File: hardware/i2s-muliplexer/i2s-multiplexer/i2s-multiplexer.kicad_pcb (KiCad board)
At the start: 2 copper layers, 81 x 53.6 mm, 24 parts, among them J1 Conn_01x05, J2 Conn_01x05, J3 Conn_01x05, J4 Conn_01x05, J5 Conn_01x05, J6 Conn_01x07, J7 Conn_01x05, U1 74HC126, U2 74HC126, U3 74HC126, U4 74HC126, U5 74HC126, U6 74HC126, U7 74LS138

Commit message: Added test point
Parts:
- removed the REF** at (96.5, 35.6)
- removed the REF** at (24.6, 35.6)
- removed the REF** at (24.1, 79.8)
- removed the REF** at (96.3, 80.0)
- added REF**: MountingHole_3.2mm_M3_ISO7380, MountingHole:MountingHole_3.2mm_M3_ISO7380, F.Cu at (24.4, 80.0)
- added REF**: MountingHole_3.2mm_M3_ISO7380, MountingHole:MountingHole_3.2mm_M3_ISO7380, F.Cu at (24.4, 34.0)
- added REF**: MountingHole_3.2mm_M3_ISO7380, MountingHole:MountingHole_3.2mm_M3_ISO7380, F.Cu at (98.0, 35.6)
- added REF**: MountingHole_3.2mm_M3_ISO7380, MountingHole:MountingHole_3.2mm_M3_ISO7380, F.Cu at (98.0, 80.0)
- added TP1: TP_GND, Connector_PinHeader_2.54mm:PinHeader_1x01_P2.54mm_Vertical, F.Cu at (86.6, 37.1)
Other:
- board size 81 x 53.6 mm -> 80.5 x 53.6 mm
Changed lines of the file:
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@@
     (tracks 546)
     (zones 0)
-    (modules 24)
+    (modules 25)
     (nets 46)
   )
@@
   )
   (module MountingHole:MountingHole_3.2mm_M3_ISO7380 (layer F.Cu)
-    (at 96.52 35.56)
+    (at 24.384 80.01)
     (descr "Mounting Hole 3.2mm, no annular, M3, ISO7380")
     (tags "mounting hole 3.2mm no annular m3 iso7380")
@@
   )
   (module MountingHole:MountingHole_3.2mm_M3_ISO7380 (layer F.Cu)
-    (at 24.638 35.56)
+    (at 24.384 34.036)
     (descr "Mounting Hole 3.2mm, no annular, M3, ISO7380")
     (tags "mounting hole 3.2mm no annular m3 iso7380")
@@
   )
   (module MountingHole:MountingHole_3.2mm_M3_ISO7380 (layer F.Cu)
-    (at 24.13 79.756)
+    (at 98.044 35.56)
     (descr "Mounting Hole 3.2mm, no annular, M3, ISO7380")
     (tags "mounting hole 3.2mm no annular m3 iso7380")
@@
   )
   (module MountingHole:MountingHole_3.2mm_M3_ISO7380 (layer F.Cu)
-    (at 96.266 80.01)
+    (at 98.044 80.01)
     (descr "Mounting Hole 3.2mm, no annular, M3, ISO7380")
     (tags "mounting hole 3.2mm no annular m3 iso7380")
@@
     )
     (pad 1 np_thru_hole circle (at 0 0) (size 3.2 3.2) (drill 3.2) (layers *.Cu *.Mask))
+  )
+  (module Connector_PinHeader_2.54mm:PinHeader_1x01_P2.54mm_Vertical (layer F.Cu)
+    (at 86.614 37.084)
+    (descr "Through hole straight pin header, 1x01, 2.54mm pitch, single row")
+    (tags "Through hole pin header THT 1x01 2.54mm single row")
+    (fp_text reference TP1 (at 0 -2.33) (layer F.SilkS)
+      (effects (font (size 1 1) (thickness 0.15)))
+    )
+    (fp_text value TP_GND (at 0 2.33) (layer F.Fab) hide
+      (effects (font (size 1 1) (thickness 0.15)))
+    )
+    (fp_text user %R (at 0 0 90) (layer F.Fab)
+      (effects (font (size 1 1) (thickness 0.15)))
+    )
+    (fp_line (start 1.8 -1.8) (end -1.8 -1.8) (layer F.CrtYd) (width 0.05))
+    (fp_line (start 1.8 1.8) (end 1.8 -1.8) (layer F.CrtYd) (width 0.05))
+    (fp_line (start -1.8 1.8) (end 1.8 1.8) (layer F.CrtYd) (width 0.05))
+    (fp_line (start -1.8 -1.8) (end -1.8 1.8) (layer F.CrtYd) (width 0.05))
+    (fp_line (start -1.33 -1.33) (end 0 -1.33) (layer F.SilkS) (width 0.12))
+    (fp_line (start -1.33 0) (end -1.33 -1.33) (layer F.SilkS) (width 0.12))
+    (fp_line (start -1.33 1.27) (end 1.33 1.27) (layer F.SilkS) (width 0.12))
+    (fp_line (start 1.33 1.27) (end 1.33 1.33) (layer F.SilkS) (width 0.12))
+    (fp_line (start -1.33 1.27) (end -1.33 1.33) (layer F.SilkS) (width 0.12))
+    (fp_line (start -1.33 1.33) (end 1.33 1.33) (layer F.SilkS) (width 0.12))
+    (fp_line (start -1.27 -0.635) (end -0.635 -1.27) (layer F.Fab) (width 0.1))
+    (fp_line (start -1.27 1.27) (end -1.27 -0.635) (layer F.Fab) (width 0.1))
+    (fp_line (start 1.27 1.27) (end -1.27 1.27) (layer F.Fab) (width 0.1))
+    (fp_line (start 1.27 -1.27) (end 1.27 1.27) (layer F.Fab) (width 0.1))
+    (fp_line (start -0.635 -1.27) (end 1.27 -1.27) (layer F.Fab) (width 0.1))
+    (pad 1 thru_hole rect (at 0 0) (size 1.7 1.7) (drill 1) (layers *.Cu *.Mask)
+      (net 21 GND))
+    (model ${KISYS3DMOD}/Connector_PinHeader_2.54mm.3dshapes/PinHeader_1x01_P2.54mm_Vertical.wrl
+      (at (xyz 0 0 0))
+      (scale (xyz 1 1 1))
+      (rotate (xyz 0 0 0))
+    )
   )
   (module Package_SO:SOIC-16_3.9x9.9mm_P1.27mm (layer F.Cu)
@@
     )
   )
+  (gr_text GND (at 84.074 36.83 90) (layer F.SilkS)
+    (effects (font (size 0.7 0.7) (thickness 0.15)))
+  )
   (gr_line (start 100.076 58.674) (end 96.266 58.674) (layer F.SilkS) (width 0.12))
   (gr_line (start 100.076 56.134) (end 100.076 58.674) (layer F.SilkS) (width 0.12))
@@
     (effects (font (size 0.7 0.7) (thickness 0.15)))
   )
-  (gr_line (start 20.574 84.074) (end 20.828 84.074) (layer Edge.Cuts) (width 0.05))
-  (gr_line (start 20.574 30.48) (end 20.574 84.074) (layer Edge.Cuts) (width 0.05))
-  (gr_line (start 101.6 30.48) (end 20.574 30.48) (layer Edge.Cuts) (width 0.05))
+  (gr_line (start 21.082 30.48) (end 21.082 84.074) (layer Edge.Cuts) (width 0.05))
+  (gr_line (start 101.6 30.48) (end 21.082 30.48) (layer Edge.Cuts) (width 0.05))
   (gr_line (start 101.6 84.074) (end 101.6 30.48) (layer Edge.Cuts) (width 0.05))
-  (gr_line (start 20.828 84.074) (end 101.6 84.074) (layer Edge.Cuts) (width 0.05))
+  (gr_line (start 21.082 84.074) (end 101.6 84.074) (layer Edge.Cuts) (width 0.05))
   (gr_text GND (at 67.564 80.518 90) (layer F.SilkS)
     (effects (font (size 1 1) (thickness 0.15)))
@@
     (polygon
       (pts
-        (xy 92.202 75.946) (xy 92.202 83.312) (xy 99.822 83.312) (xy 99.822 75.946)
+        (xy 93.726 76.2) (xy 93.726 83.566) (xy 101.346 83.566) (xy 101.346 76.2)
       )
     )
@@
     (polygon
       (pts
-        (xy 20.574 76.2) (xy 27.686 76.2) (xy 27.686 83.058) (xy 20.574 83.058)
+        (xy 21.082 76.708) (xy 27.686 76.708) (xy 27.686 83.312) (xy 21.082 83.312)
       )
     )
@@
     (polygon
       (pts
-        (xy 21.59 32.258) (xy 27.686 32.258) (xy 27.686 38.862) (xy 21.59 38.862)
+        (xy 21.336 30.734) (xy 27.432 30.734) (xy 27.432 37.338) (xy 21.336 37.338)
       )
     )
@@
     (polygon
       (pts
-        (xy 93.218 32.258) (xy 99.822 32.258) (xy 99.822 39.116) (xy 93.218 39.116)
+        (xy 94.742 32.258) (xy 101.346 32.258) (xy 101.346 39.116) (xy 94.742 39.116)
       )
     )

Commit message: Moved component together
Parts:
- moved J6 2.79 mm to (67.8, 73.2)
- moved R6 2.79 mm to (66.0, 68.1)
- moved U7 2.79 mm to (74.9, 65.5)
- moved REF** 2.59 mm to (97.5, 77.5)
- moved U4 2.59 mm to (36.5, 65.8)
- moved J5 2.59 mm to (30.2, 73.4)
- moved REF** 2.55 mm to (24.6, 77.5)
- moved J4 2.54 mm to (46.2, 73.4)
- moved U5 2.54 mm to (52.4, 65.8)
- moved REF** 1.52 mm to (98.0, 34.0)
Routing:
- net /LRCLK: track 149.0 -> 141.1 mm
- net /CH_EN_0: track 64.4 -> 56.6 mm
- net /CH_EN_1: track 86.4 -> 78.7 mm
- net /DATA: track 95.4 -> 88.3 mm
- net /BCLK: track 120.3 -> 116.1 mm
- net /MCLK: track 122.5 -> 118.7 mm
- net /MCLK_EN: track 39.8 -> 37.0 mm
- net /CH_EN_2: track 93.1 -> 90.3 mm
- net /CH_EN_3: track 86.5 -> 84.1 mm
- net /CH_EN_4: track 57.6 -> 55.3 mm
- net /DATA_1: track 11.8 -> 12.3 mm
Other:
- board size 80.5 x 53.6 mm -> 80.5 x 50.8 mm

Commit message: Tuned i2s input tracks
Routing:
- net /LRCLK_2: track 6.29 -> 11.9 mm
- net /LRCLK_1: track 6.29 -> 11.8 mm
- net /LRCLK_0: track 6.46 -> 11.8 mm
- net /LRCLK_3: track 6.75 -> 12.0 mm
- net /LRCLK_4: track 7.34 -> 12.4 mm
- net /CH_EN_3: track 84.1 -> 79.1 mm, vias 7 -> 8
- net /CH_EN_2: track 90.3 -> 85.9 mm, vias 6 -> 7
- net /MCLK_1: track 8.86 -> 11.8 mm
- net /MCLK_0: track 9.14 -> 11.9 mm
- net /MCLK_4: track 10.2 -> 12.6 mm
- net /CH_EN_4: track 55.3 -> 53.2 mm, vias 7 -> 6
- net /MCLK_3: track 9.62 -> 11.7 mm
- net /BCLK_1: track 12.1 -> 14.1 mm
- net /MCLK_2: track 9.92 -> 11.9 mm
- net /BCLK_4: track 11.6 -> 12.6 mm

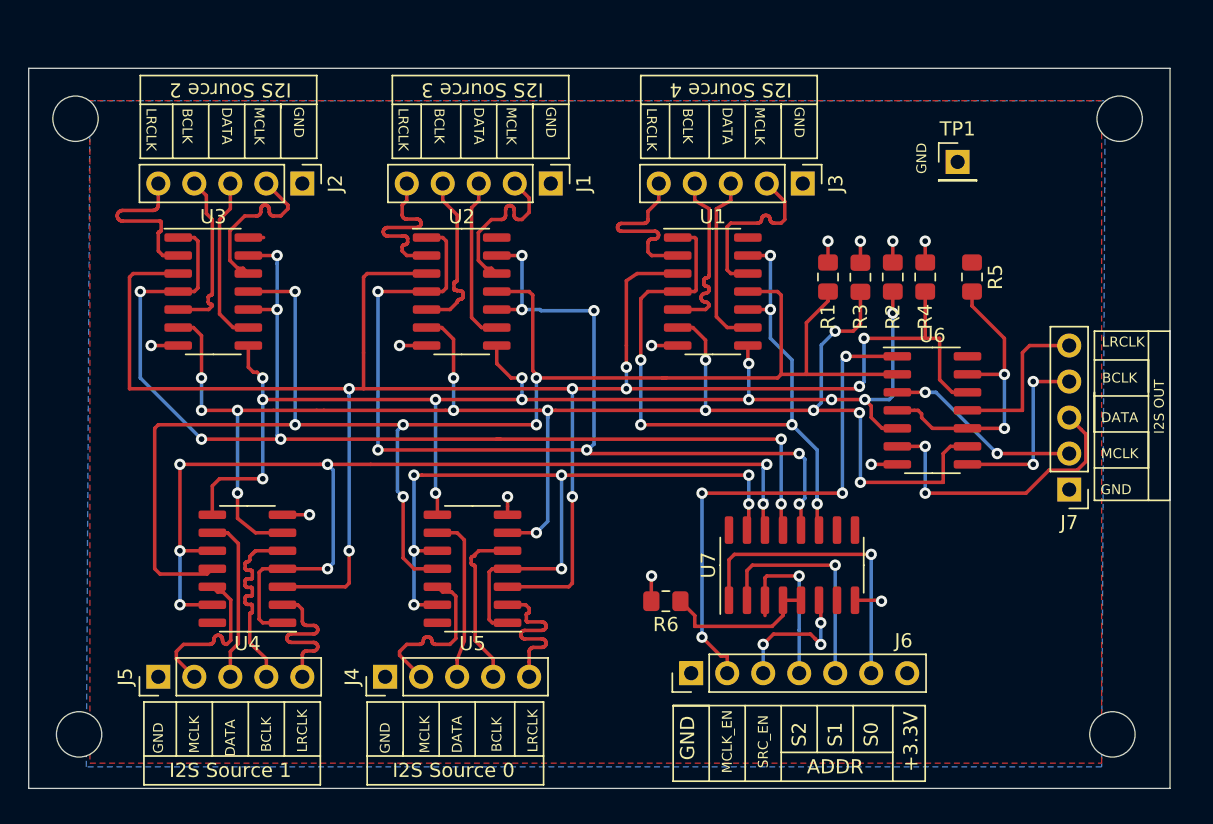
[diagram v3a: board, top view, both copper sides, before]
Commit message: Rationalised bus structure
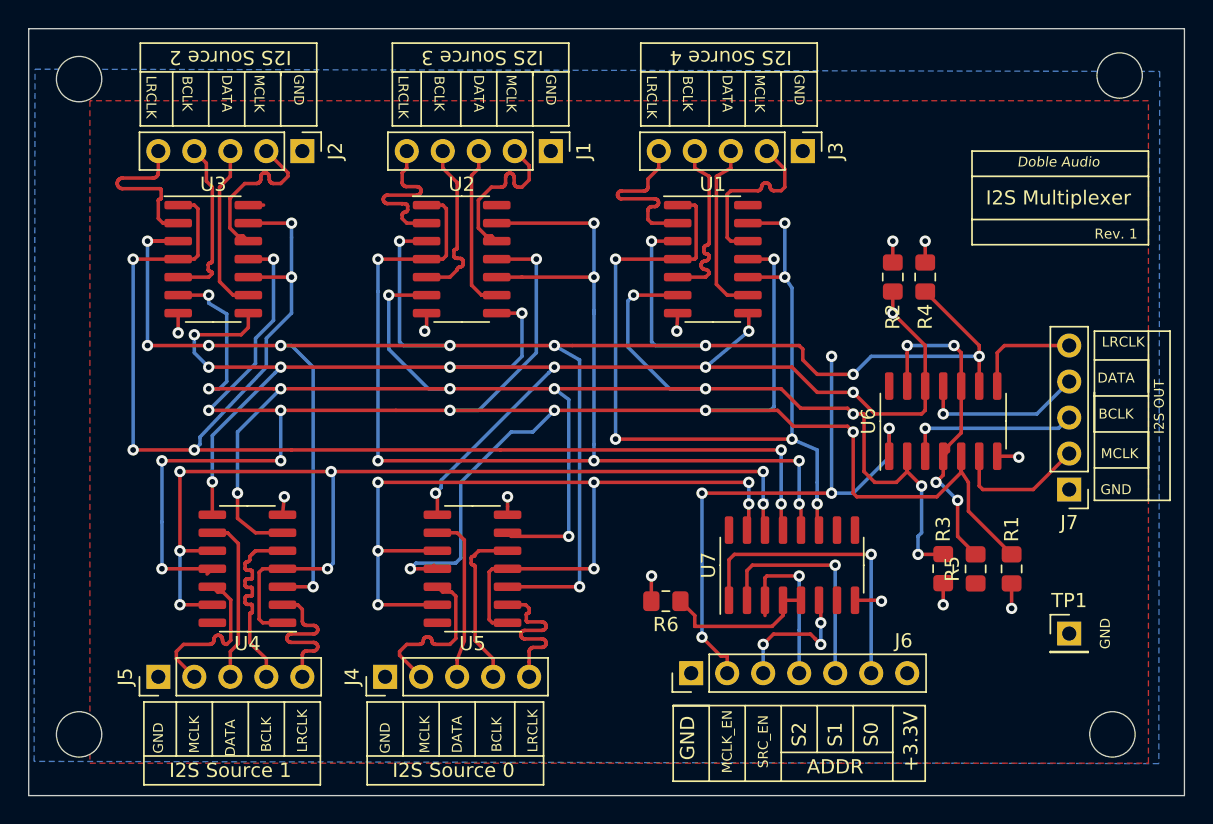
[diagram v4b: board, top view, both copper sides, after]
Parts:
- moved TP1 34.2 mm to (94.5, 70.4)
- moved R1 24.3 mm to (90.4, 65.8), turned to 90 degrees
- moved R3 21.4 mm to (85.6, 65.8), turned to 90 degrees
- moved R5 20.6 mm to (87.9, 65.8), turned to 90 degrees
- moved REF** 3.05 mm to (98.0, 31.0)
- moved REF** 2.81 mm to (24.6, 31.2)
- moved U1 2.29 mm to (69.3, 43.9)
- moved U2 2.29 mm to (51.6, 43.9)
- moved U3 2.29 mm to (34.1, 43.9)
- moved J1 2.29 mm to (57.9, 36.3)
- moved J2 2.29 mm to (40.4, 36.3)
- moved J3 2.29 mm to (75.7, 36.3)
- moved U6 1.08 mm to (85.6, 55.4), turned to 90 degrees
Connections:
- J7 pad 3: /DATA_OUT -> /BCLK_OUT
- J7 pad 4: /BCLK_OUT -> /DATA_OUT
- U6 pad 11: /LRCLK_OUT -> /DATA_OUT
- U6 pad 12: /LRCLK -> /DATA
- U6 pad 2: /MCLK -> /BCLK
- U6 pad 3: /MCLK_OUT -> /BCLK_OUT
- U6 pad 5: /DATA -> /MCLK
- U6 pad 6: /DATA_OUT -> /MCLK_OUT
- U6 pad 8: /BCLK_OUT -> /LRCLK_OUT
- U6 pad 9: /BCLK -> /LRCLK
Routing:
- net /MCLK: track 118.7 -> 159.8 mm, vias 6 -> 13
- net /DATA: track 88.3 -> 111.3 mm
- net /BCLK: track 116.1 -> 131.0 mm, vias 14 -> 13
- net /CH_EN_2: track 85.9 -> 99.2 mm
- net /CH_EN_4: track 53.2 -> 64.6 mm
- net /CH_EN_3: track 79.1 -> 89.3 mm, vias 8 -> 7
- net /DATA_OUT: track 21.1 -> 11.8 mm, vias 2 -> 1
- net /LRCLK: track 141.1 -> 149.9 mm, vias 8 -> 13
- net /CH_EN_0: track 56.6 -> 64.9 mm
- net /MCLK_EN: track 37.0 -> 41.6 mm, vias 4 -> 5
- net /MCLK_OUT: track 13.9 -> 9.60 mm, vias 2 -> 0
- net /LRCLK_OUT: track 11.5 -> 7.64 mm
- net GND: track 20.4 -> 18.4 mm
- net Net-(R5-Pad2): track 21.4 -> 23.1 mm, vias 2 -> 4
- net /CH_EN_1: track 78.7 -> 77.5 mm
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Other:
- board size 80.5 x 50.8 mm -> 81.5 x 54.1 mm
- board text added: "Doble Audio"
- board text added: "I2S Multiplexer"
- board text added: "Rev. 1"

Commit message: Minor routing changes
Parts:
- moved U1 49.0 mm to (113.0, 66.0)
- moved U3 49.0 mm to (77.8, 66.0)
- moved U2 49.0 mm to (95.3, 66.0)
- moved J3 49.0 mm to (119.4, 58.4)
- moved J5 49.0 mm to (73.9, 95.5)
- moved J6 49.0 mm to (111.5, 95.2)
- moved R2 49.0 mm to (125.7, 67.3)
- moved R3 49.0 mm to (129.3, 87.9)
- moved R5 49.0 mm to (131.6, 87.9)
- moved REF** 49.0 mm to (141.7, 53.1)
- moved U6 49.0 mm to (129.3, 77.5)
- moved J1 49.0 mm to (101.6, 58.4)
- moved J2 49.0 mm to (84.1, 58.4)
- moved J4 49.0 mm to (89.9, 95.5)
- moved J7 49.0 mm to (138.2, 82.3)
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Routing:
- net /LRCLK: track 149.9 -> 150.9 mm
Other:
- board text added: "Decoupling caps"
- board text added: "Output signals need to tuned"
- board text added: "Position mounting holes"
- board text added: "TO DO"

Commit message: Initial placement
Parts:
- removed the REF** at (68.3, 99.6)
- removed the REF** at (141.7, 53.1)
- removed the REF** at (141.2, 99.6)
- removed U6: 74HC126, Package_SO:SOIC-14_3.9x8.7mm_P1.27mm
- removed U7: 74LS138, Package_SO:SOIC-16_3.9x9.9mm_P1.27mm
- added C1: 10u, Capacitor_SMD:C_0805_2012Metric_Pad1.15x1.40mm_HandSolder, F.Cu at (44.2, 147.6)
- added C10: 100n, Capacitor_SMD:C_0805_2012Metric_Pad1.15x1.40mm_HandSolder, F.Cu at (100.8, 160.3)
- added C2: 100n, Capacitor_SMD:C_0805_2012Metric_Pad1.15x1.40mm_HandSolder, F.Cu at (46.2, 147.6)
- added C3: 10u, Capacitor_SMD:C_0805_2012Metric_Pad1.15x1.40mm_HandSolder, F.Cu at (80.0, 153.7)
- added C4: 10u, Capacitor_SMD:C_0805_2012Metric_Pad1.15x1.40mm_HandSolder, F.Cu at (75.9, 147.6)
- added C5: 100n, Capacitor_SMD:C_0805_2012Metric_Pad1.15x1.40mm_HandSolder, F.Cu at (80.0, 155.7)
- added C6: 100n, Capacitor_SMD:C_0805_2012Metric_Pad1.15x1.40mm_HandSolder, F.Cu at (78.0, 147.6)
- added C7: 10u, Capacitor_SMD:C_0805_2012Metric_Pad1.15x1.40mm_HandSolder, F.Cu at (33.0, 158.7)
- added C8: 10u, Capacitor_SMD:C_0805_2012Metric_Pad1.15x1.40mm_HandSolder, F.Cu at (98.8, 160.3)
- added C9: 100n, Capacitor_SMD:C_0805_2012Metric_Pad1.15x1.40mm_HandSolder, F.Cu at (31.0, 158.7)
- added J8: Conn_01x05, Connector_PinHeader_2.54mm:PinHeader_1x05_P2.54mm_Vertical, F.Cu at (104.1, 159.5)
- added R7: 10K, Resistor_SMD:R_0805_2012Metric_Pad1.15x1.40mm_HandSolder, F.Cu at (36.3, 159.0)
- added REF**: MountingHole_3.2mm_M3_ISO7380, MountingHole:MountingHole_3.2mm_M3_ISO7380, F.Cu at (30.0, 171.0)
- added REF**: MountingHole_3.2mm_M3_ISO7380, MountingHole:MountingHole_3.2mm_M3_ISO7380, F.Cu at (101.6, 171.0)
- added REF**: MountingHole_3.2mm_M3_ISO7380, MountingHole:MountingHole_3.2mm_M3_ISO7380, F.Cu at (29.7, 130.0)
- J6: value Conn_01x07 -> Conn_01x05; footprint Connector_PinHeader_2.54mm:PinHeader_1x07_P2.54mm_Vertical -> Connector_PinHeader_2.54mm:PinHeader_1x05_P2.54mm_Vertical
- J7: value Conn_01x05 -> Conn_01x07; footprint Connector_PinHeader_2.54mm:PinHeader_1x05_P2.54mm_Vertical -> Connector_PinHeader_2.54mm:PinHeader_1x07_P2.54mm_Vertical
- U1, U2, U3: value 74HC126 -> 74HC244; footprint Package_SO:SOIC-14_3.9x8.7mm_P1.27mm -> Package_SO:SOIC-20W_7.5x12.8mm_P1.27mm
- U5: value 74HC126 -> 74LS138; footprint Package_SO:SOIC-14_3.9x8.7mm_P1.27mm -> Package_SO:SOIC-16_3.9x9.9mm_P1.27mm
- moved J7 126.4 mm to (27.7, 143.8), turned to 0 degrees
- moved R2 104.2 mm to (62.5, 150.1), turned to 90 degrees
- moved R4 103.0 mm to (66.8, 150.1), turned to 90 degrees
- moved U2 99.0 mm to (77.0, 163.3)
- moved R1 96.4 mm to (60.5, 150.1), turned to 270 degrees
- moved R3 89.7 mm to (64.8, 150.1)
- moved U5 89.0 mm to (33.8, 151.4)
- moved J1 85.5 mm to (53.1, 128.8), turned to 90 degrees
- moved J6 84.7 mm to (79.8, 173.7)
- moved REF** 83.6 mm to (101.7, 130.0)
- moved R5 83.4 mm to (98.8, 164.6)
- moved U1 79.9 mm to (79.8, 138.7), turned to 180 degrees
- moved J2 78.8 mm to (48.5, 128.8)
- moved J3 78.6 mm to (82.3, 127.8), turned to 90 degrees
- moved J5 78.2 mm to (74.4, 173.7), turned to 270 degrees
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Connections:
- net /LRCLK_4 renamed LRCLK_3
- J1 pad 2: /MCLK_3 -> MCLK_5
- J1 pad 3: /DATA_3 -> DATA_5
- J1 pad 4: /BCLK_3 -> BCLK_5
- J1 pad 5: /LRCLK_3 -> LRCLK_5
- J2 pad 2: /MCLK_2 -> MCLK_4
- J2 pad 3: /DATA_2 -> DATA_4
- J2 pad 4: /BCLK_2 -> BCLK_4
- J2 pad 5: /LRCLK_2 -> LRCLK_4
- J3 pad 2: /MCLK_4 -> MCLK_3
- J3 pad 3: /DATA_4 -> DATA_3
- J3 pad 4: /BCLK_4 -> BCLK_3
- J4 pad 2: /MCLK_0 -> MCLK_2
- J4 pad 3: /DATA_0 -> DATA_2
- J4 pad 4: /BCLK_0 -> BCLK_2
- J4 pad 5: /LRCLK_0 -> LRCLK_2
- J5 pad 2: /MCLK_1 -> MCLK_1
- J5 pad 3: /DATA_1 -> DATA_1
- J5 pad 4: /BCLK_1 -> BCLK_1
- J5 pad 5: /LRCLK_1 -> LRCLK_1
- J6 pad 2: /MCLK_EN -> MCLK_0
- J6 pad 3: /SRC_EN -> DATA_0
- J6 pad 4: /S2 -> BCLK_0
- J6 pad 5: /S1 -> LRCLK_0
- J7 pad 2: /MCLK_OUT -> MCLK_EN
- J7 pad 3: /BCLK_OUT -> SRC_EN
- J7 pad 4: /DATA_OUT -> A2
- J7 pad 5: /LRCLK_OUT -> A1
- R1 pad 2: /MCLK -> /LRCLK
- R2 pad 2: /DATA -> /BCLK
- R3 pad 2: /BCLK -> /DATA
- R4 pad 2: /LRCLK -> /MCLK
- R6 pad 1: Net-(R6-Pad1) -> MCLK_OUT
- U1 pad 1: /CH_EN_4 -> /CH_EN_3
- U1 pad 10: /CH_EN_4 -> GND
- U1 pad 11: /MCLK -> MCLK_2
- U1 pad 12: /MCLK_4 -> /MCLK
- U1 pad 13: /CH_EN_4 -> DATA_2
- U1 pad 14: +3V3 -> /DATA
- U1 pad 4: /CH_EN_4 -> BCLK_3
- U1 pad 5: /BCLK_4 -> /BCLK
- U1 pad 6: /BCLK -> DATA_3
- U1 pad 7: GND -> /DATA
- U1 pad 8: /DATA -> MCLK_3
- U1 pad 9: /DATA_4 -> /MCLK
- U2 pad 1: /CH_EN_3 -> /CH_EN_1
- U2 pad 10: /CH_EN_3 -> GND
- U2 pad 11: /MCLK -> MCLK_0
- U2 pad 12: /MCLK_3 -> /MCLK
- U2 pad 13: /CH_EN_3 -> DATA_0
- U2 pad 14: +3V3 -> /DATA
- U2 pad 2: /LRCLK_3 -> LRCLK_1
- U2 pad 4: /CH_EN_3 -> BCLK_1
- U2 pad 5: /BCLK_3 -> /BCLK
- U2 pad 6: /BCLK -> DATA_1
- U2 pad 7: GND -> /DATA
- U2 pad 8: /DATA -> MCLK_1
- U2 pad 9: /DATA_3 -> /MCLK
- U3 pad 1: /CH_EN_2 -> /CH_EN_5
- U3 pad 10: /CH_EN_2 -> GND
- U3 pad 11: /MCLK -> MCLK_4
- U3 pad 12: /MCLK_2 -> /MCLK
- U3 pad 13: /CH_EN_2 -> DATA_4
- U3 pad 14: +3V3 -> /DATA
- U3 pad 2: /LRCLK_2 -> LRCLK_5
- U3 pad 4: /CH_EN_2 -> BCLK_5
- U3 pad 5: /BCLK_2 -> /BCLK
- U3 pad 6: /BCLK -> DATA_5
- U3 pad 7: GND -> /DATA
- U3 pad 8: /DATA -> MCLK_5
- U3 pad 9: /DATA_2 -> /MCLK
- U4 pad 1: /CH_EN_1 -> MCLK_EN
- U4 pad 10: /CH_EN_1 -> Net-(R5-Pad2)
- U4 pad 11: /MCLK -> LRCLK_OUT
- U4 pad 12: /MCLK_1 -> /LRCLK
- U4 pad 13: /CH_EN_1 -> Net-(R5-Pad2)
- U4 pad 2: /LRCLK_1 -> /MCLK
- U4 pad 3: /LRCLK -> MCLK_OUT
- U4 pad 4: /CH_EN_1 -> Net-(R5-Pad2)
- U4 pad 5: /BCLK_1 -> /DATA
- U4 pad 6: /BCLK -> DATA_OUT
- U4 pad 8: /DATA -> BCLK_OUT
- U4 pad 9: /DATA_1 -> /BCLK
- U5 pad 1: /CH_EN_0 -> A0
- U5 pad 10: /CH_EN_0 -> /CH_EN_5
- U5 pad 11: /MCLK -> /CH_EN_4
- U5 pad 12: /MCLK_0 -> /CH_EN_3
- U5 pad 13: /CH_EN_0 -> /CH_EN_2
- U5 pad 14: +3V3 -> /CH_EN_1
- U5 pad 2: /LRCLK_0 -> A1
- U5 pad 3: /LRCLK -> A2
- U5 pad 4: /CH_EN_0 -> Net-(R7-Pad1)
- U5 pad 5: /BCLK_0 -> Net-(R7-Pad1)
- U5 pad 6: /BCLK -> SRC_EN
- U5 pad 7: GND -> Net-(U5-Pad7)
- U5 pad 8: /DATA -> GND
- U5 pad 9: /DATA_0 -> Net-(U5-Pad9)
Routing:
- net /CH_EN_2: track 99.2 -> 0.00 mm, vias 7 -> 0
- net /CH_EN_3: track 89.3 -> 0.00 mm, vias 7 -> 0
- net /MCLK: track 159.3 -> 72.4 mm, vias 13 -> 0
- net /LRCLK: track 150.9 -> 72.7 mm, vias 13 -> 0
- net /CH_EN_1: track 77.5 -> 0.00 mm, vias 7 -> 0
- net /CH_EN_0: track 64.9 -> 0.00 mm, vias 7 -> 0
- net /CH_EN_4: track 64.6 -> 0.00 mm, vias 6 -> 0
- net /BCLK: track 130.5 -> 67.3 mm, vias 13 -> 0
- net /MCLK_EN: track 41.6 -> 0.00 mm, vias 5 -> 0
- net /DATA: track 111.0 -> 71.2 mm, vias 12 -> 0
- net Net-(R5-Pad2): track 23.1 -> 0.00 mm, vias 4 -> 0
- net /S0: track 21.4 -> 0.00 mm, vias 1 -> 0
- net LRCLK_5: track 0.00 -> 20.6 mm, vias 0 -> 1
- net LRCLK_4: track 0.00 -> 18.7 mm
- net BCLK_5: track 0.00 -> 18.2 mm, vias 0 -> 1
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- removed copper zone on F.Cu, net +3V3
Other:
- board size 81.5 x 54.1 mm -> 80 x 50 mm
- net class Power added: clearance 0.45, trace_width 0.5, via_dia 1.5, via_drill 0.7
- board text removed: "BCLK"
- board text removed: "DATA"
- board text removed: "Decoupling caps"
- board text removed: "I2S OUT"
- board text removed: "I2S Source 0"
- board text removed: "I2S Source 1"
- board text removed: "I2S Source 2"
- board text removed: "I2S Source 3"
- board text removed: "I2S Source 4"
- board text removed: "LRCLK"
- board text removed: "MCLK"
- board text removed: "Output signals need to tuned"
- board text removed: "Position mounting holes"
- board text removed: "TO DO"
